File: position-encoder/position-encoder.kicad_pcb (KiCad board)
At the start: 2 copper layers, 65 x 15 mm, 11 parts, among them J1 Conn_01x04_Male, U1 TLE4905L, U2 TLE4905L

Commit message: Update PCB
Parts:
- moved R2 4.47 mm to (158.1, 85.9), turned to 0 degrees
- moved R1 0.81 mm to (146.7, 85.9)
- moved U1 0.63 mm to (150.5, 81.9)
- moved U2 0.63 mm to (156.8, 81.9)
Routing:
- net GND: track 47.4 -> 64.5 mm
- net Net-(C2-Pad1): track 32.1 -> 28.4 mm
- net +5V: track 47.4 -> 49.3 mm
- net Net-(C1-Pad1): track 52.4 -> 51.5 mm
- added copper zone on B.Cu, net GND
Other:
- outline, holes or cut-outs redrawn
- net class Default: trace_width 0.25 -> 0.5
- rule trace_min: 0.2 -> 0.5

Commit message: Improve PCB
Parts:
- moved C2 83.9 mm to (103.8, 139.7), turned to 180 degrees
- moved C4 74.9 mm to (108.8, 135.9), turned to 180 degrees
- moved J1 71.8 mm to (127.0, 131.4)
- moved REF** 71.8 mm to (77.6, 138.5)
- moved REF** 71.8 mm to (135.6, 138.5)
- moved U1 71.8 mm to (99.7, 132.7)
- moved U2 71.8 mm to (106.0, 132.7)
- moved C1 69.6 mm to (92.1, 134.5)
- moved C3 68.1 mm to (99.7, 135.9), turned to 180 degrees
- moved R2 64.0 mm to (111.4, 129.5), turned to 270 degrees
- moved R1 54.2 mm to (114.6, 129.5), turned to 270 degrees
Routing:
- net +5V: track 49.3 -> 37.7 mm, vias 2 -> 0
- net Net-(C1-Pad1): track 51.5 -> 43.2 mm
- net GND: track 64.5 -> 67.3 mm
- net Net-(C2-Pad1): track 28.4 -> 27.1 mm
- removed copper zone on B.Cu, net GND
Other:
- net class Power added: clearance 0.254, trace_width 1.016, via_dia 1.6, via_drill 0.8
- net class Signal added: clearance 0.254, trace_width 0.508, via_dia 1.6, via_drill 0.8
- board text added: "Maarten De Munck Earth Rover Position Encoder Rev. 1"
- board text added: "Rev. 1 Earth Rover Position Encoder"
- board text removed: "Maarten De Munck Position Encoder for Earth Rover - Rev. 1"
- board text removed: "Position Encoder for Earth Rover - Rev. 1"

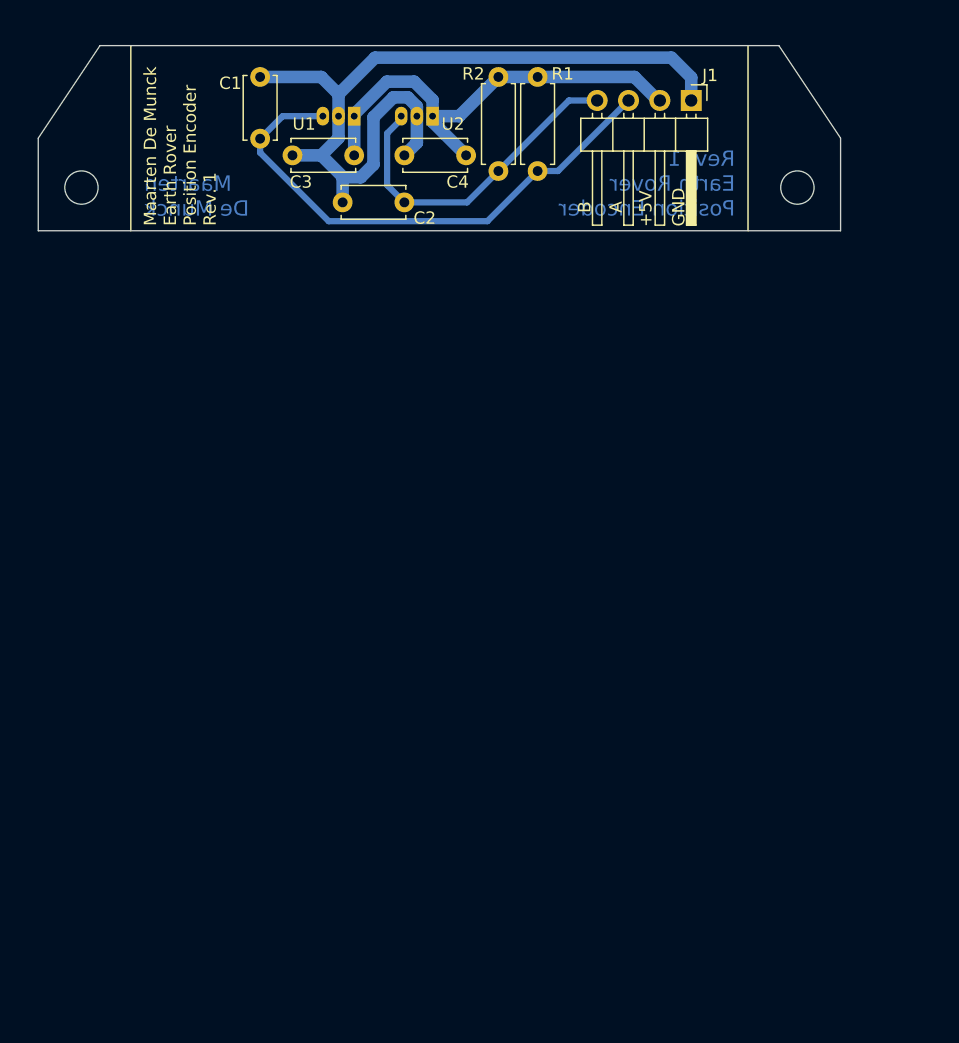
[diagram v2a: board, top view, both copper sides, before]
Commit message: Update PCB of position encoder
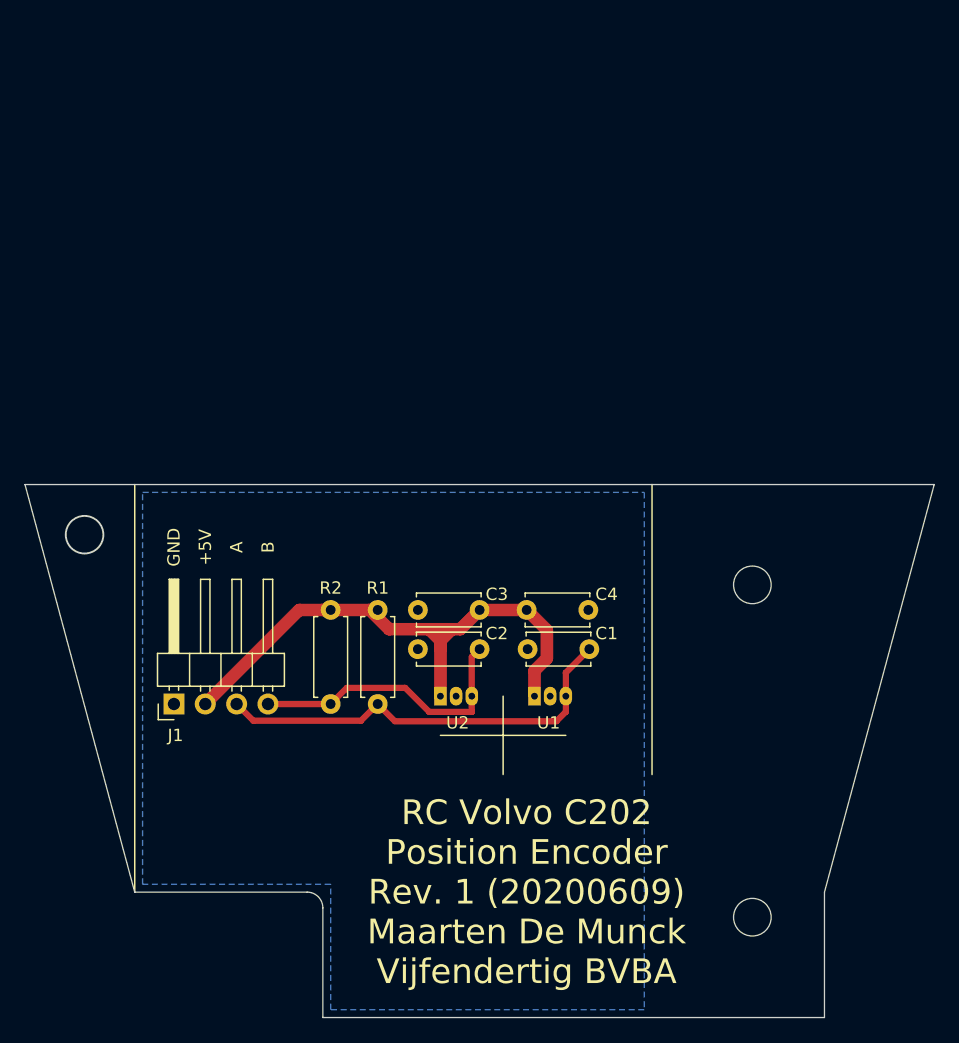
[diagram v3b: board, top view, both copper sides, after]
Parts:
- removed REF** (x2): MountingHole_2.7mm_M2.5_DIN965, MountingHole:MountingHole_2.7mm_M2.5_DIN965
- moved J1 64.4 mm to (85.1, 180.3), turned to 90 degrees
- moved C1 49.2 mm to (118.7, 175.9), turned to 180 degrees
- moved U1 49.2 mm to (114.3, 179.7), turned to 90 degrees
- moved U2 47.0 mm to (106.7, 179.7), turned to 90 degrees
- moved R2 45.3 mm to (97.8, 172.7)
- moved R1 45.1 mm to (101.6, 172.7)
- moved C3 38.2 mm to (109.9, 172.7)
- moved C4 37.2 mm to (113.7, 172.7), turned to 0 degrees
- moved C2 36.7 mm to (109.9, 175.9)
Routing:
- net GND: track 67.3 -> 0.00 mm
- net +5V: track 37.7 -> 47.5 mm
- net Net-(C1-Pad1): track 43.2 -> 34.6 mm
- net Net-(C2-Pad1): track 27.1 -> 23.2 mm
- added copper zone on B.Cu, net GND
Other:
- board size 65 x 15 mm -> 73.7 x 43.2 mm
- board text added: "RC Volvo C202 Position Encoder Rev. 1 (20200609) Maarten De Munck Vijfendertig BVBA"
- board text removed: "Maarten De Munck"
- board text removed: "Maarten De Munck Earth Rover Position Encoder Rev. 1"
- board text removed: "Rev. 1 Earth Rover Position Encoder"
